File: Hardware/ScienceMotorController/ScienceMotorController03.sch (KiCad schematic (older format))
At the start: 1 part

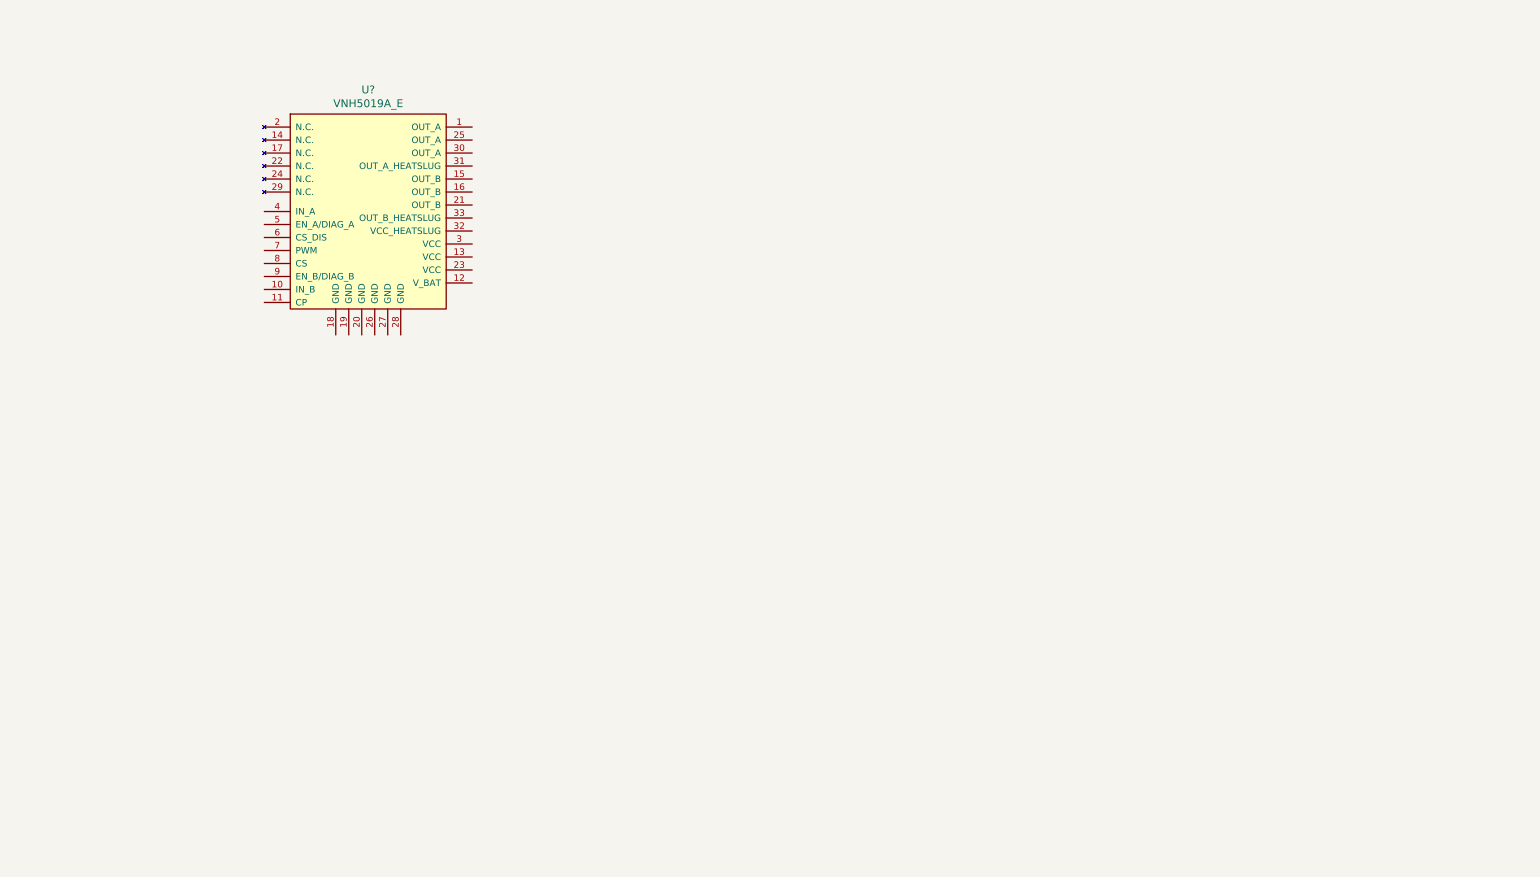
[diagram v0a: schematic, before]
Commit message: Set up VNH IC's
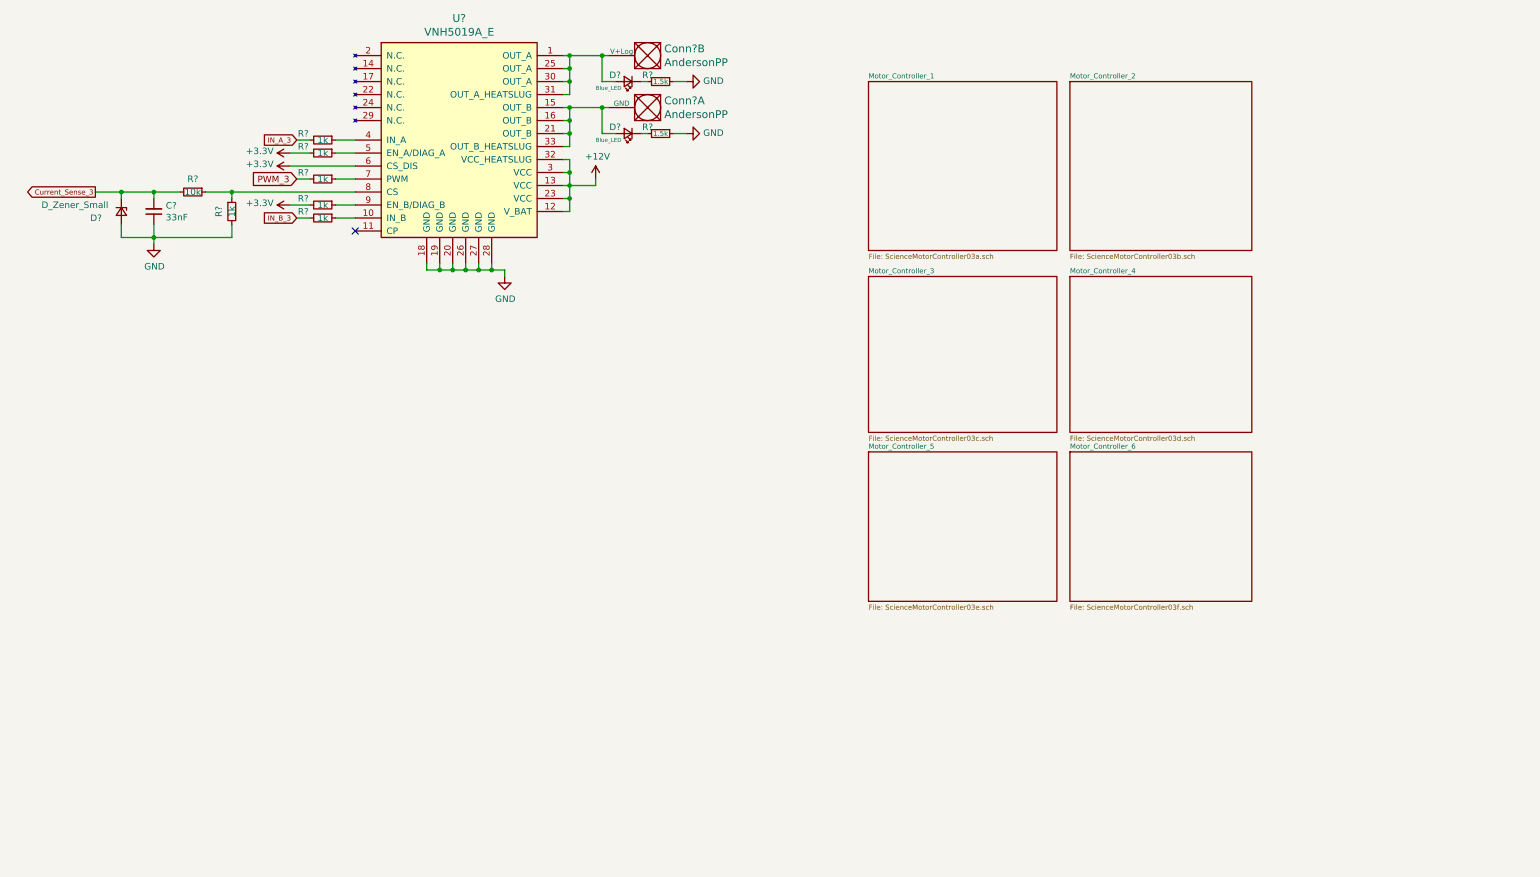
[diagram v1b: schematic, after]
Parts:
- added C?: 33nF, symbol Device:C_Small
- added Conn? (x2): AndersonPP, symbol MRDT_Connectors:AndersonPP
- added D?: D_Zener_Small, symbol Device:D_Zener_Small
- added D? (x2): Blue_LED, symbol Device:LED_Small
- added R? (x6): 1k, symbol Device:R_Small
- added R?: 10k, symbol Device:R_Small
- added R? (x2): 1.5k, symbol Device:R_Small
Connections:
- net at U?.1 (OUT_A): now also U?.25 (OUT_A), U?.30 (OUT_A), U?.31 (OUT_A_HEATSLUG), Conn?.2 (V+Log), D?.2 (A)
- net at U?.10 (IN_B): now also R?.1
- net +12V: now reaches U?.12 (V_BAT)
- net +12V: now also U?.13 (VCC), U?.23 (VCC), U?.3 (VCC), U?.32 (VCC_HEATSLUG)
- net at U?.15 (OUT_B): now also U?.16 (OUT_B), U?.21 (OUT_B), U?.33 (OUT_B_HEATSLUG), Conn?.1 (GND), D?.2 (A)
- net GND: now reaches U?.18 (GND)
- net GND: now also U?.19 (GND), U?.20 (GND), U?.26 (GND), U?.27 (GND), U?.28 (GND), C?.1, D?.2 (A), R?.1, R?.1, R?.2
- net at U?.4 (IN_A): now also R?.1
- net at U?.5 (EN_A/DIAG_A): now also R?.1
- net +3V3: now reaches U?.6 (CS_DIS)
- net +3V3: now also R?.2, R?.2
- net at U?.7 (PWM): now also R?.1
- net at U?.8 (CS): now also R?.1, R?.1
- net at U?.9 (EN_B/DIAG_B): now also R?.1
- new net: D?.1 (K), R?.2 (x2)
- new net Current_Sense_3: C?.2, D?.1 (K), R?.2
- new net IN_A_3: R?.2
- new net IN_B_3: R?.2
- new net PWM_3: R?.2
- no-connect marks 0 -> 1
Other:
- moved on the sheet: U?

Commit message: Sheet titles
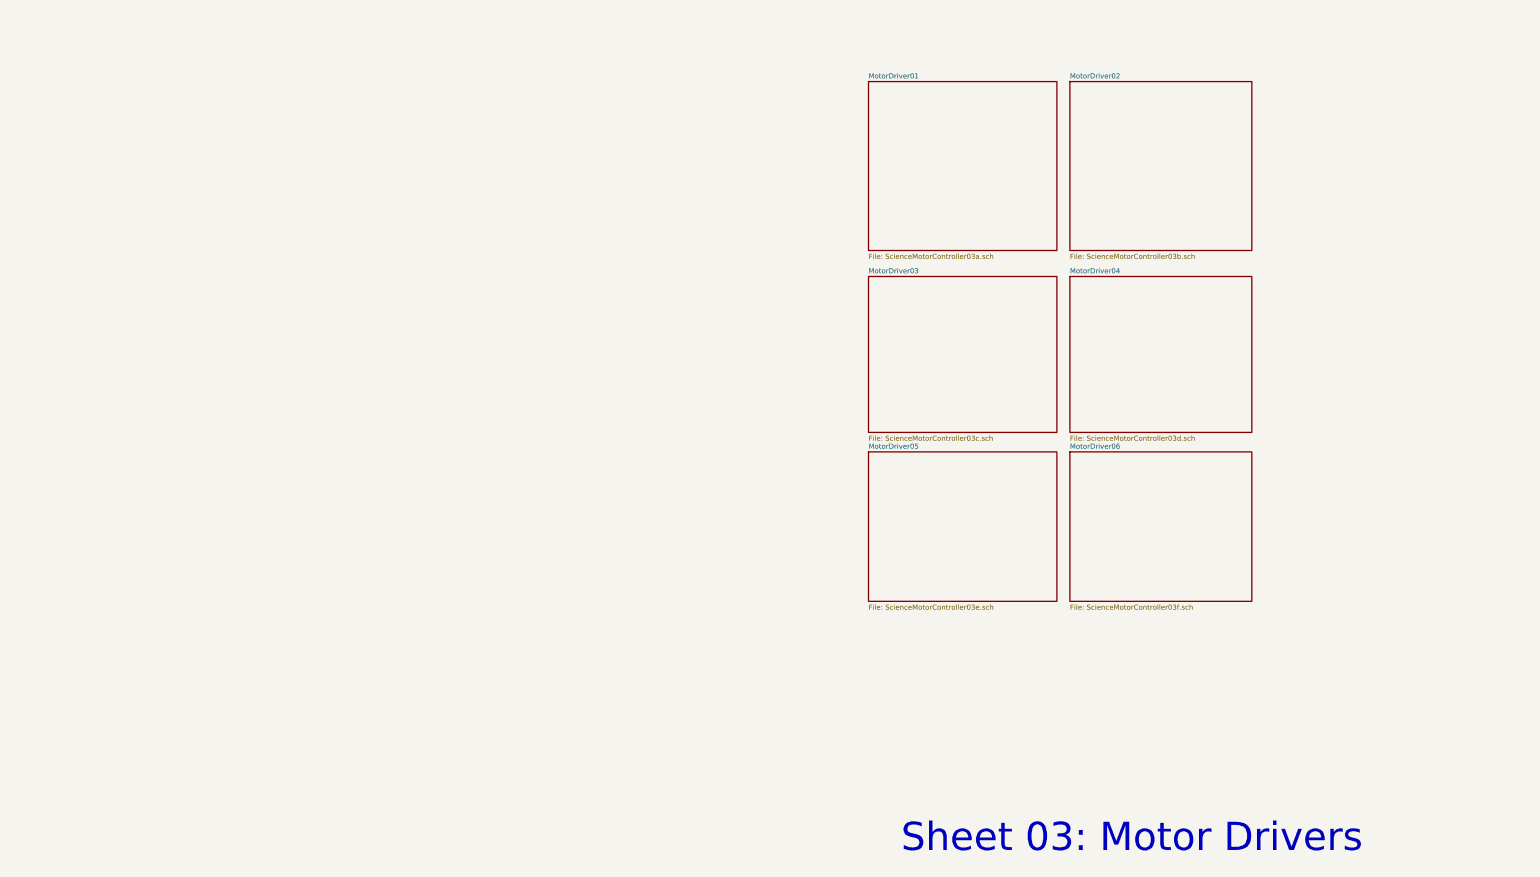
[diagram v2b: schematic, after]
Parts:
- removed C?: 33nF, symbol Device:C_Small
- removed Conn? (x2): AndersonPP, symbol MRDT_Connectors:AndersonPP
- removed D?: D_Zener_Small, symbol Device:D_Zener_Small
- removed D? (x2): Blue_LED, symbol Device:LED_Small
- removed R? (x6): 1k, symbol Device:R_Small
- removed R?: 10k, symbol Device:R_Small
- removed R? (x2): 1.5k, symbol Device:R_Small
- removed U?: VNH5019A_E, symbol MRDT_ICs:VNH5019A_E
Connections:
- no-connect marks 1 -> 0
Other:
- note added: "Sheet 03: Motor Drivers"

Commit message: limit switch indicators
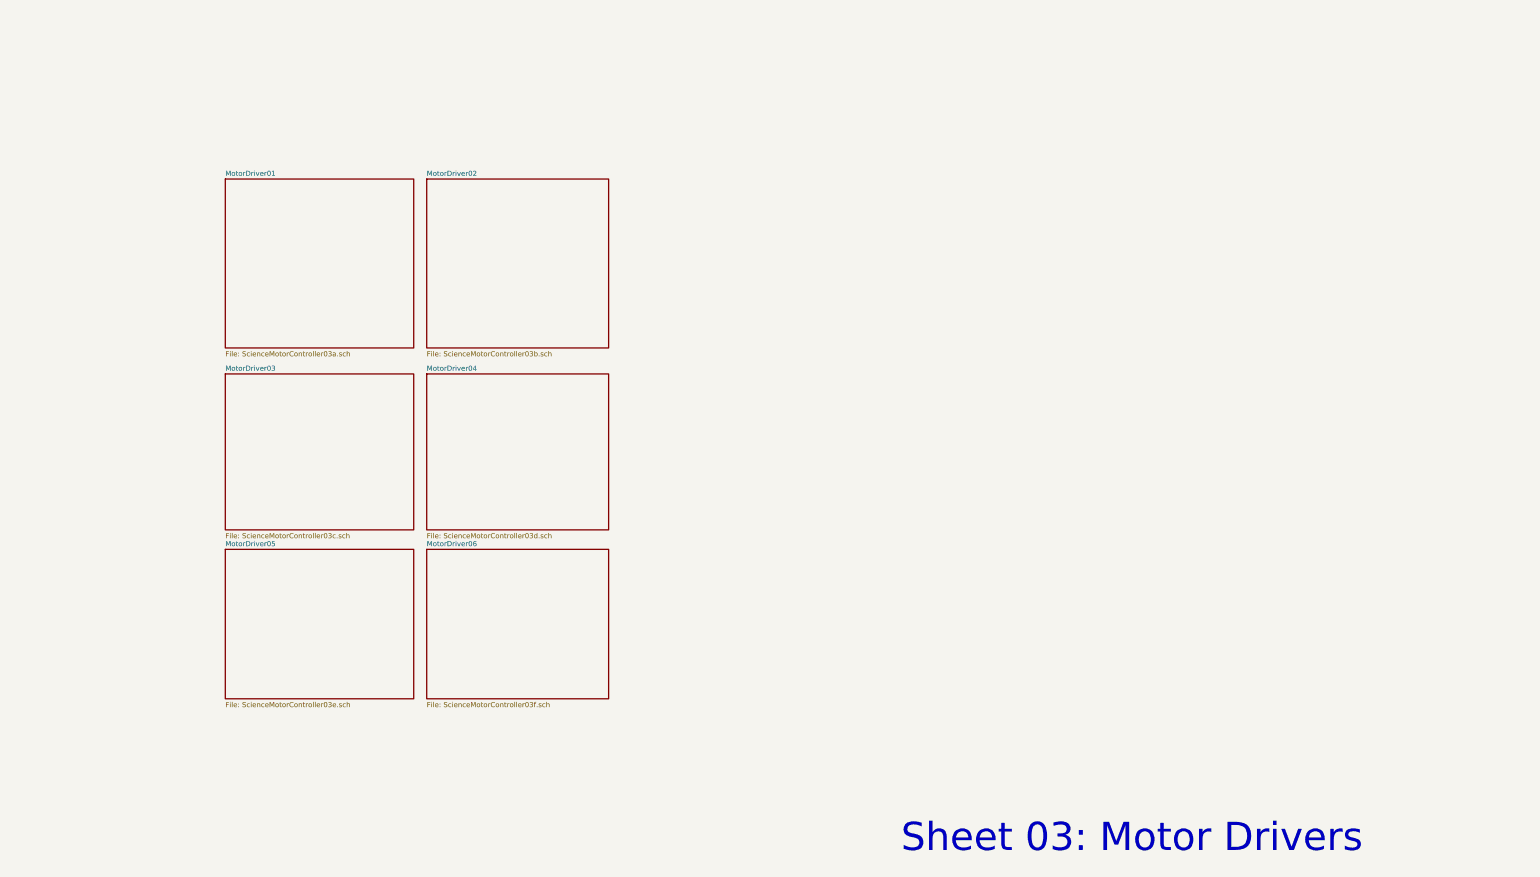
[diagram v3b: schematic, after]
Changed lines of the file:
@@
 $EndDescr
 $Sheet
-S 6950 1050 1450 1300
+S 2000 1800 1450 1300
 U 5FA0F855
 F0 "MotorDriver01" 39
@@
 $EndSheet
 $Sheet
-S 8500 1050 1400 1300
+S 3550 1800 1400 1300
 U 5FA36344
 F0 "MotorDriver02" 39
@@
 $EndSheet
 $Sheet
-S 6950 2550 1450 1200
+S 2000 3300 1450 1200
 U 5FA660A7
 F0 "MotorDriver03" 39
@@
 $EndSheet
 $Sheet
-S 8500 2550 1400 1200
+S 3550 3300 1400 1200
 U 5FA6640B
 F0 "MotorDriver04" 39
@@
 $EndSheet
 $Sheet
-S 6950 3900 1450 1150
+S 2000 4650 1450 1150
 U 5FA666AF
 F0 "MotorDriver05" 39
@@
 $EndSheet
 $Sheet
-S 8500 3900 1400 1150
+S 3550 4650 1400 1150
 U 5FA66A7C
 F0 "MotorDriver06" 39

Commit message: changed everything to actuation, added schottky diode, added A/B flags to tiva
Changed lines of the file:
@@
 S 3550 4650 1400 1150
 U 5FA66A7C
-F0 "MotorDriver06" 39
+F0 "MixerOutput" 39
 F1 "ScienceMotorController03f.sch" 39
 $EndSheet
